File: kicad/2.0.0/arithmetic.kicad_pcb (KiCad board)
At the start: 2 copper layers, 38.4 x 55.2 mm, 69 parts, among them J1 Conn_01x03_Male, J2 Conn_01x05_Female, J3 Conn_01x05_Female, J4 Conn_Coaxial, J5 Conn_Coaxial, J6 Conn_Coaxial, U1 LM317, U2 LM337, U3 OPA2197xD, U4 OPA197xDBV

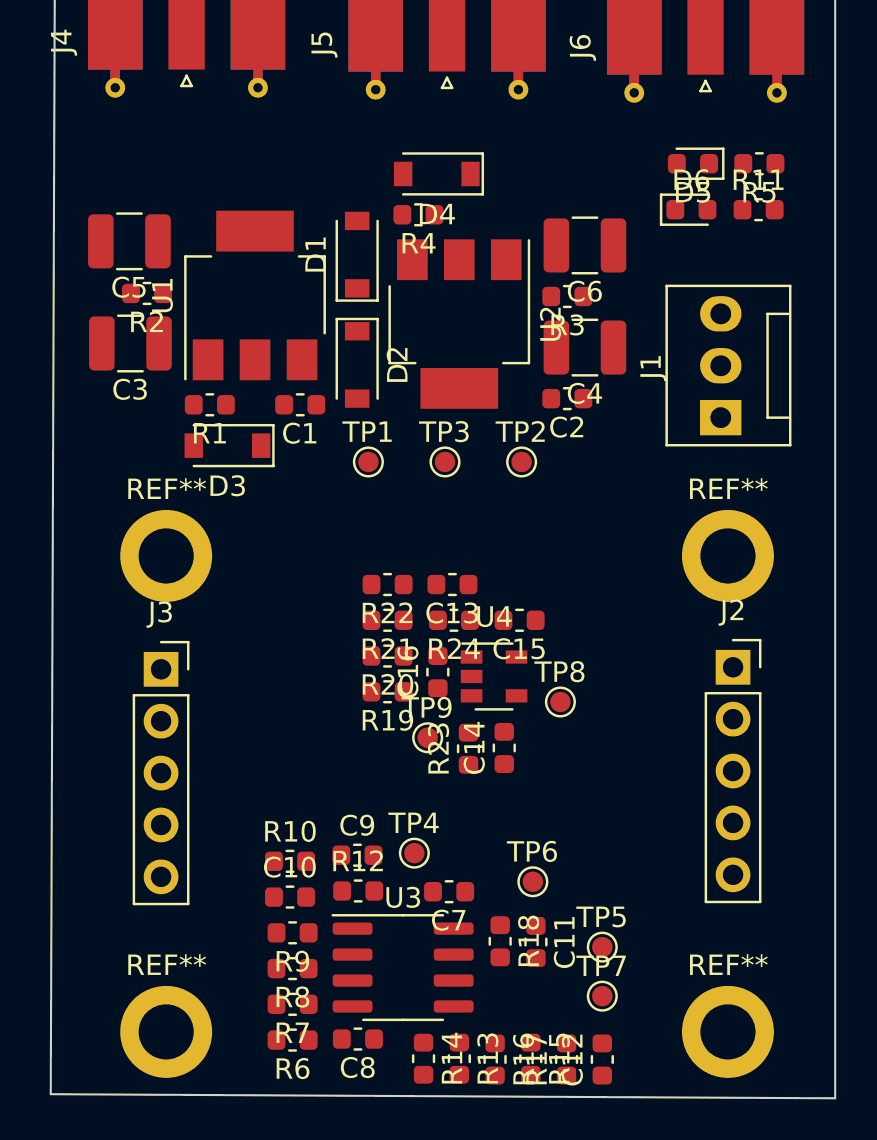
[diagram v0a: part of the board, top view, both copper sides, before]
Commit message: routed traces for 2.0.0 pcbs
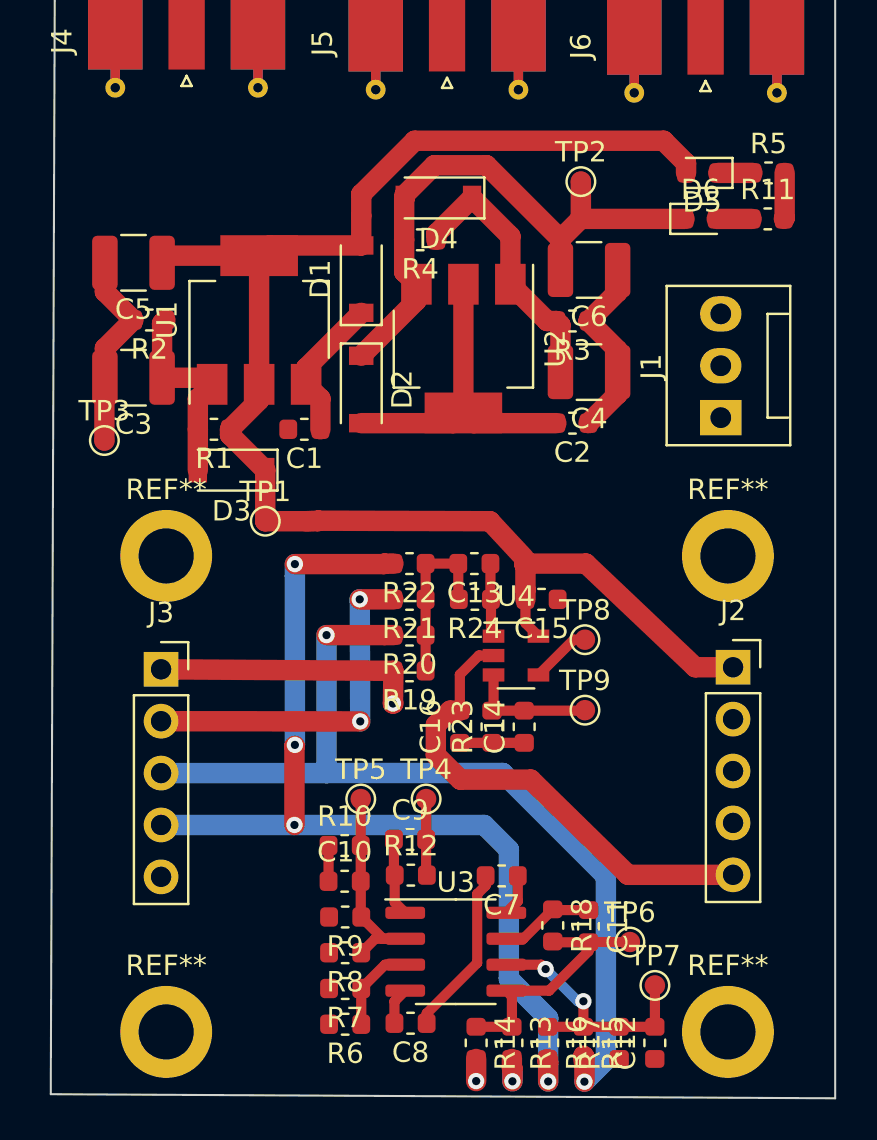
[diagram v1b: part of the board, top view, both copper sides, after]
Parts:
- moved TP3 16.7 mm to (201.2, 82.4)
- moved TP2 14.0 mm to (224.6, 69.7)
- moved TP5 13.9 mm to (213.8, 100.0)
- moved TP9 7.82 mm to (224.8, 95.6)
- moved TP1 5.82 mm to (209.1, 86.3)
- moved TP6 5.59 mm to (226.9, 107.0)
- moved TP8 3.28 mm to (224.8, 92.2)
- moved C16 2.88 mm to (218.6, 96.4)
- moved C10 2.79 mm to (213.0, 104.0)
- moved R10 2.79 mm to (213.0, 102.2)
- moved TP4 2.71 mm to (217.0, 100.0)
- moved R16 2.70 mm to (222.9, 111.9)
- moved R17 2.70 mm to (226.4, 111.9)
- moved C12 2.70 mm to (228.2, 111.9)
- moved C11 2.69 mm to (224.9, 106.2)
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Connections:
- J3 pad 2: /-X2 -> /-Y1
- J3 pad 3: /-Y1 -> /-X2
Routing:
- net +12V: track 0.00 -> 77.2 mm
- net -12V: track 0.00 -> 54.3 mm
- net /-Y2: track 0.00 -> 48.4 mm, vias 0 -> 4
- net /-X2: track 0.00 -> 45.8 mm, vias 0 -> 2
- net GND: track 0.00 -> 34.7 mm
- net /-Y1: track 0.00 -> 18.5 mm, vias 0 -> 3
- net -15V: track 0.00 -> 16.3 mm
- net /-X1: track 0.00 -> 14.7 mm, vias 0 -> 2
- net Net-(C4-Pad2): track 0.00 -> 13.4 mm
- net Net-(C12-Pad2): track 0.00 -> 13.2 mm, vias 0 -> 2
- net Net-(C11-Pad2): track 0.00 -> 12.7 mm
- net Net-(C13-Pad2): track 0.00 -> 11.6 mm
- net Net-(C10-Pad2): track 0.00 -> 10.8 mm
- net Net-(C3-Pad1): track 0.00 -> 9.97 mm
- net Net-(C9-Pad2): track 0.00 -> 8.12 mm
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
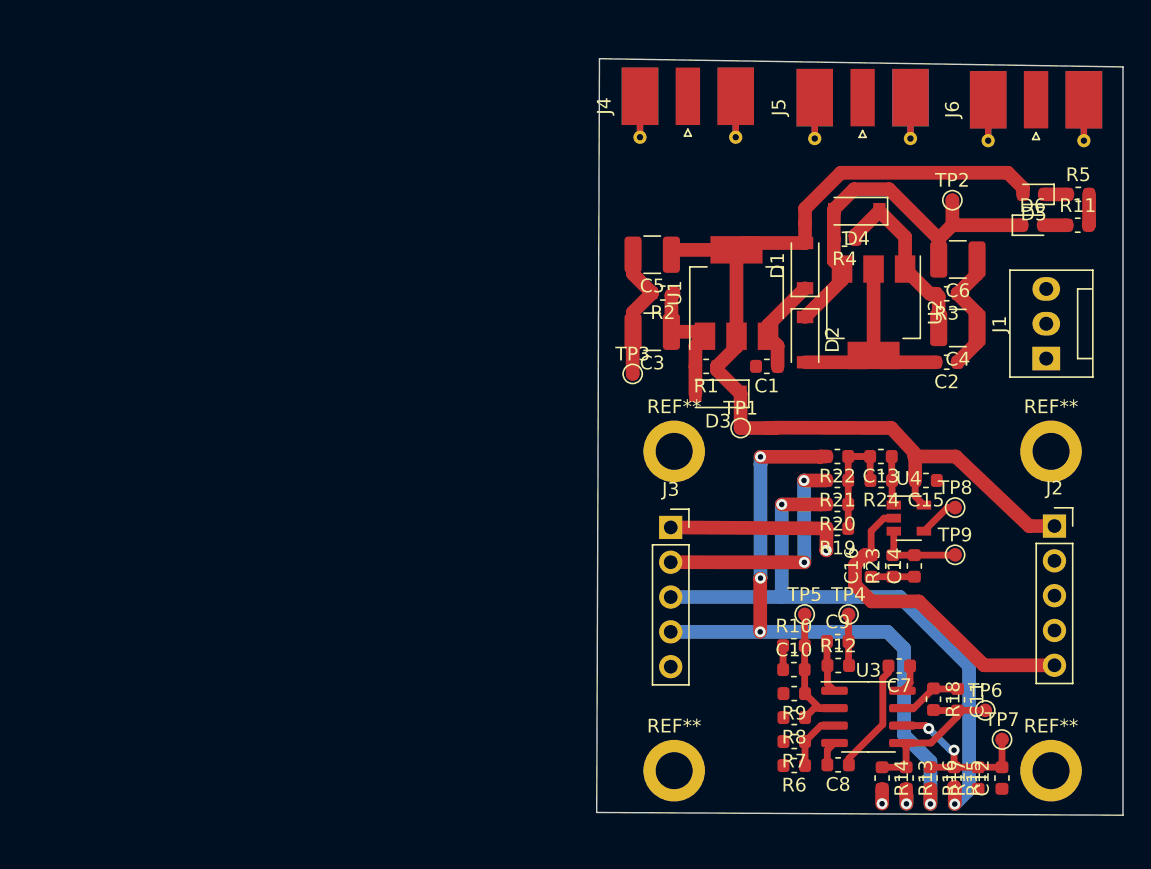
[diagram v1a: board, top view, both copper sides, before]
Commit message: replaced dual op-amp on 2.0.0 arithmetic board with two op-amps
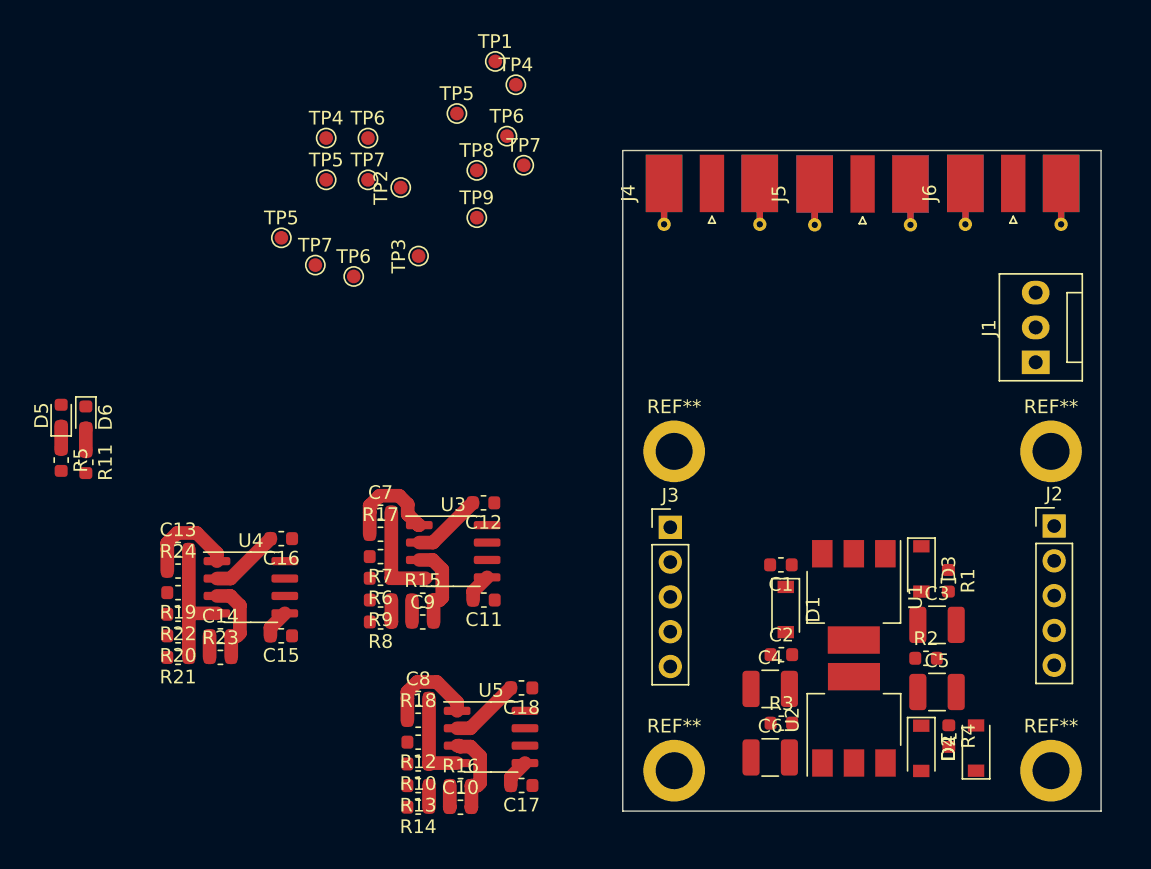
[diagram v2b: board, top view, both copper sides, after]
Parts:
- added C17: 100n, Capacitor_SMD:C_0603_1608Metric, F.Cu at (193.1, 112.4)
- added C18: 100n, Capacitor_SMD:C_0603_1608Metric, F.Cu at (193.1, 105.3)
- added TP4: DIFFX+, TestPoint:TestPoint_Pad_D1.0mm, F.Cu at (178.9, 65.2)
- added TP5: DIFFX-, TestPoint:TestPoint_Pad_D1.0mm, F.Cu at (175.6, 72.5)
- added TP5: DIFFY+, TestPoint:TestPoint_Pad_D1.0mm, F.Cu at (178.9, 68.2)
- added TP6: DIFFY-, TestPoint:TestPoint_Pad_D1.0mm, F.Cu at (180.9, 75.3)
- added TP6: DIFFX-, TestPoint:TestPoint_Pad_D1.0mm, F.Cu at (181.9, 65.2)
- added TP7: DIFFY+, TestPoint:TestPoint_Pad_D1.0mm, F.Cu at (178.1, 74.5)
- added TP7: DIFFY-, TestPoint:TestPoint_Pad_D1.0mm, F.Cu at (181.9, 68.2)
- added U5: OPA197xDBV, Package_SO:SOIC-8_3.9x4.9mm_P1.27mm, F.Cu at (190.9, 108.9)
- C11, C12: value 5p -> 100n
- C7, C8: value 100n -> 5p
- J2, J3: value Conn_01x05_Female -> Conn_01x05_Male; footprint Connector_PinSocket_2.54mm:PinSocket_1x05_P2.54mm_Vertical -> Connector_PinHeader_2.54mm:PinHeader_1x05_P2.54mm_Vertical
- U3: value OPA2197xD -> OPA197xDBV
- U4: footprint Package_TO_SOT_SMD:SOT-23-5 -> Package_SO:SOIC-8_3.9x4.9mm_P1.27mm
- moved R5 76.7 mm to (159.5, 88.7), turned to 270 degrees
- moved R11 74.4 mm to (161.3, 88.8), turned to 270 degrees
- moved D5 72.8 mm to (159.5, 85.4), turned to 90 degrees
- moved D6 70.5 mm to (161.3, 85.6), turned to 270 degrees
- moved TP7 54.5 mm to (193.3, 67.2)
- moved TP6 54.5 mm to (192.1, 65.0)
- moved R24 51.7 mm to (168.1, 96.8), turned to 0 degrees
- moved C13 51.7 mm to (168.1, 95.2), turned to 0 degrees
- moved C14 50.9 mm to (171.1, 101.5), turned to 0 degrees
- moved R21 49.8 mm to (168.1, 103.1)
- moved R23 49.5 mm to (171.1, 103.1), turned to 0 degrees
- moved R22 49.5 mm to (168.1, 99.9)
- moved R20 49.1 mm to (168.1, 101.5)
- moved C15 48.4 mm to (175.6, 101.5)
- moved R19 48.3 mm to (168.1, 98.4)
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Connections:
- C11 pad 1: /DIFFY -> GND
- C11 pad 2: Net-(C11-Pad2) -> +12V
- C12 pad 2: Net-(C12-Pad2) -> -12V
- C7 pad 1: +12V -> /DIFFX
- C7 pad 2: GND -> Net-(C7-Pad2)
- C8 pad 1: GND -> /DIFFY
- C8 pad 2: -12V -> Net-(C8-Pad2)
- C9 pad 1: /DIFFX -> GND
- R10 pad 1: GND -> Net-(C8-Pad2)
- R10 pad 2: Net-(C10-Pad2) -> /-X2
- R12 pad 1: /DIFFX -> Net-(C8-Pad2)
- R12 pad 2: Net-(C9-Pad2) -> /-Y2
- R13 pad 1: Net-(C11-Pad2) -> Net-(C10-Pad2)
- R14 pad 1: Net-(C11-Pad2) -> Net-(C10-Pad2)
- R15 pad 1: Net-(C12-Pad2) -> GND
- R15 pad 2: /-X2 -> Net-(C9-Pad2)
- R16 pad 1: Net-(C12-Pad2) -> GND
- R16 pad 2: /-Y2 -> Net-(C10-Pad2)
- R17 pad 1: GND -> /DIFFX
- R17 pad 2: Net-(C12-Pad2) -> Net-(C7-Pad2)
- R18 pad 2: Net-(C11-Pad2) -> Net-(C8-Pad2)
- R6 pad 1: Net-(C9-Pad2) -> Net-(C7-Pad2)
- R6 pad 2: /-X1 -> /-X2
- R7 pad 1: Net-(C9-Pad2) -> Net-(C7-Pad2)
- R7 pad 2: /-Y2 -> /-Y1
- R8 pad 1: Net-(C10-Pad2) -> Net-(C9-Pad2)
- R8 pad 2: /-X2 -> /-X1
- R9 pad 1: Net-(C10-Pad2) -> Net-(C9-Pad2)
- R9 pad 2: /-Y1 -> /-Y2
- U3 pad 2: Net-(C10-Pad2) -> -12V
- U3 pad 4: -12V -> Net-(C7-Pad2)
- U3 pad 5: Net-(C11-Pad2) -> +12V
- U3 pad 6: Net-(C12-Pad2) -> (no net)
- U3 pad 7: /DIFFY -> (no net)
- U3 pad 8: +12V -> (no net)
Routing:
- net +12V: track 77.2 -> 6.22 mm
- net /-Y2: track 48.4 -> 0.00 mm, vias 4 -> 0
- net /-X2: track 45.8 -> 0.00 mm, vias 2 -> 0
- net -12V: track 54.3 -> 15.3 mm
- net GND: track 34.7 -> 4.75 mm
- net /-Y1: track 18.5 -> 0.00 mm, vias 3 -> 0
- net -15V: track 16.3 -> 0.00 mm
- net /-X1: track 14.7 -> 0.00 mm, vias 2 -> 0
- net Net-(C4-Pad2): track 13.4 -> 0.00 mm
- net Net-(C12-Pad2): track 13.2 -> 0.00 mm, vias 2 -> 0
- net Net-(C11-Pad2): track 12.7 -> 0.00 mm
- net Net-(C3-Pad1): track 9.97 -> 0.00 mm
- net Net-(C7-Pad2): track 0.00 -> 7.31 mm
- net +15V: track 7.11 -> 0.00 mm
- net Net-(C8-Pad2): track 0.00 -> 6.86 mm
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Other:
- board size 38.4 x 55.2 mm -> 34.9 x 48.2 mm

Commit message: improved arithmetic 2.0.0 pcb
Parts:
- removed the REF** at (204.2, 88.0)
- removed the REF** at (204.2, 111.3)
- removed the TP6 at (192.1, 65.0)
- removed the TP6 at (181.9, 65.2)
- removed the TP7 at (193.3, 67.2)
- removed the TP7 at (181.9, 68.2)
- added REF**: MountingHole_2.7mm_M2.5_ISO7380_Pad, MountingHole:MountingHole_2.7mm_M2.5_ISO7380_Pad, F.Cu at (78.0, 105.8)
- added REF**: MountingHole_2.7mm_M2.5_ISO7380_Pad, MountingHole:MountingHole_2.7mm_M2.5_ISO7380_Pad, F.Cu at (78.0, 129.2)
- added TP7: DIFFY-, TestPoint:TestPoint_Pad_D1.0mm, F.Cu at (112.7, 98.0)
- R1, R2, R3, R4: footprint Resistor_SMD:R_0603_1608Metric -> Resistor_SMD:R_1210_3225Metric
- TP4: value DIFFX+ -> DIFFX-
- TP5: value DIFFX- -> DIFFX+
- TP6: value DIFFY- -> DIFFY+
- TP7: value DIFFY+ -> DIFFY-
- TP8: value SUM+ -> SUM-
- TP9: value SUM- -> SUM+
- moved J6 147.1 mm to (82.3, 77.4)
- moved C3 136.6 mm to (87.3, 111.9), turned to 180 degrees
- moved C5 136.1 mm to (87.3, 105.3), turned to 180 degrees
- moved R2 135.4 mm to (87.3, 108.6), turned to 180 degrees
- moved D4 135.1 mm to (88.3, 127.5)
- moved R4 133.6 mm to (91.9, 126.8), turned to 0 degrees
- moved R1 133.1 mm to (92.0, 111.9), turned to 180 degrees
- moved D3 131.6 mm to (91.9, 114.8), turned to 180 degrees
- moved D2 128.8 mm to (98.1, 122.7)
- moved J3 127.5 mm to (77.7, 111.4)
- moved REF** 127.5 mm to (105.5, 129.2)
- moved REF** 127.5 mm to (105.5, 105.8)
- moved J2 127.5 mm to (105.7, 111.3)
- moved C6 126.9 mm to (85.5, 127.5), turned to 270 degrees
- moved J1 126.2 mm to (113.0, 127.3), turned to 0 degrees
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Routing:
- net /-Y2: track 0.00 -> 61.8 mm, vias 0 -> 3
- net /-Y1: track 0.00 -> 60.3 mm, vias 0 -> 3
- net /-X2: track 0.00 -> 58.1 mm, vias 0 -> 3
- net /-X1: track 0.00 -> 57.0 mm, vias 0 -> 3
- net +12V: track 6.22 -> 53.6 mm
- net -15V: track 0.00 -> 43.0 mm, vias 0 -> 2
- net +15V: track 0.00 -> 37.0 mm, vias 0 -> 2
- net -12V: track 15.3 -> 50.8 mm
- net GND: track 4.75 -> 32.5 mm
- net Net-(C4-Pad2): track 0.00 -> 15.9 mm
- net Net-(C3-Pad1): track 0.00 -> 13.7 mm
- net /SUM: track 7.16 -> 14.4 mm
- net /DIFFY: track 7.23 -> 14.4 mm
- net /DIFFX: track 7.32 -> 14.4 mm
- net Net-(C9-Pad2): track 7.91 -> 11.8 mm
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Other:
- board size 34.9 x 48.2 mm -> 50 x 55 mm

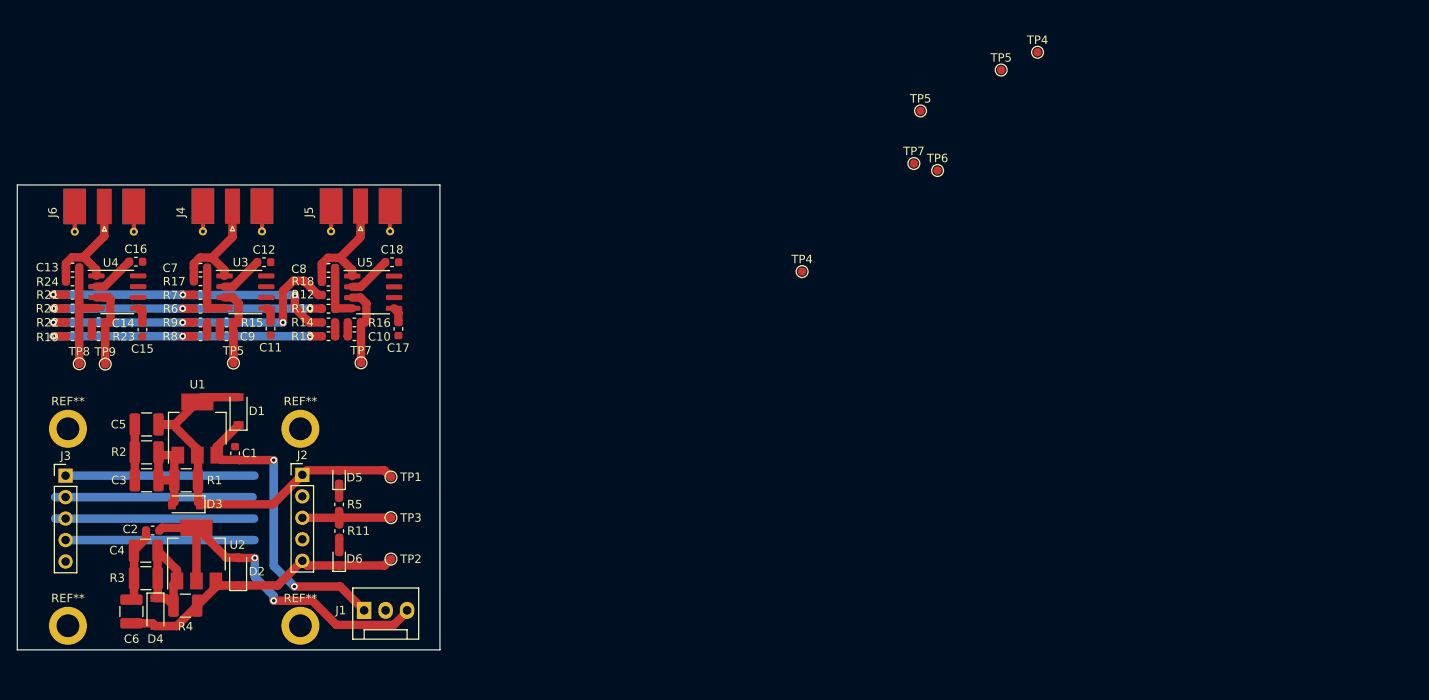
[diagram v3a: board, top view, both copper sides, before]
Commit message: completed signal tracing for arithmetic 2.0.0 board
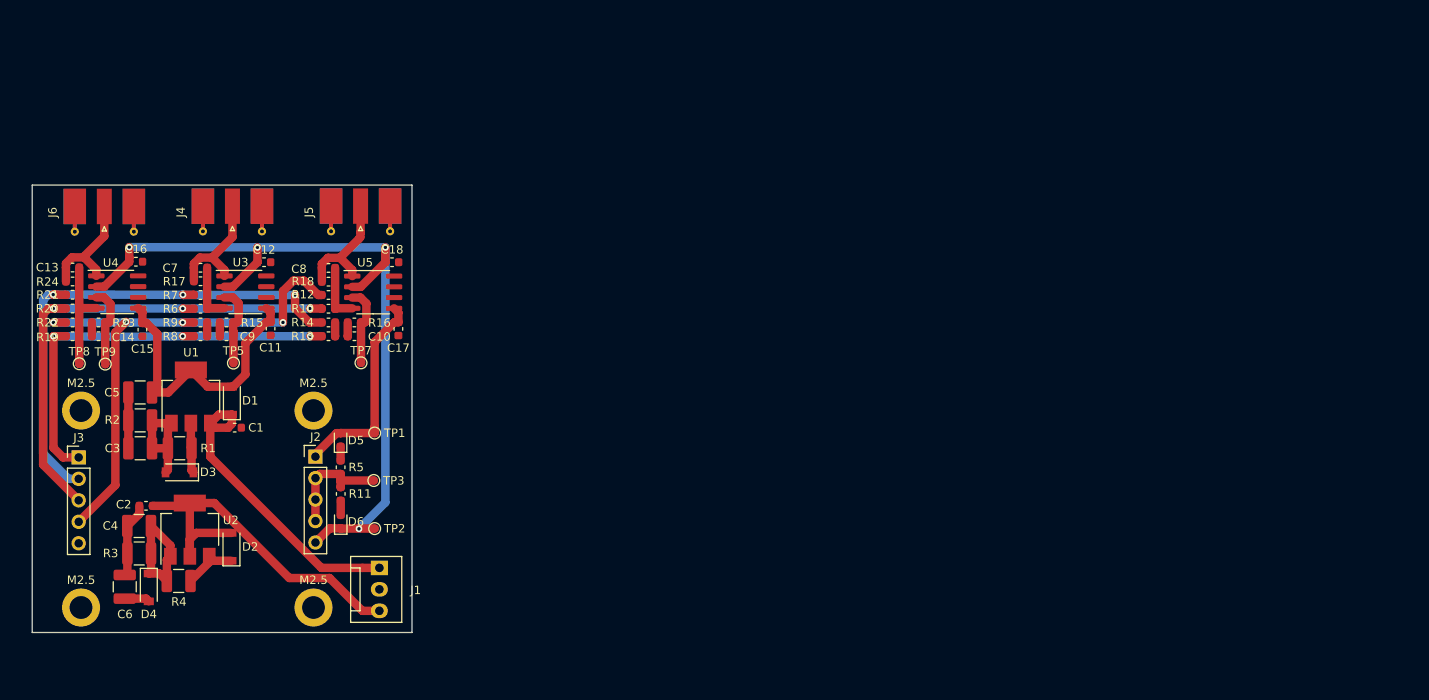
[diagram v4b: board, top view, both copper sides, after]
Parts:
- removed TP4: DIFFX-, TestPoint:TestPoint_Pad_D1.0mm
- removed TP4: DIFFX+, TestPoint:TestPoint_Pad_D1.0mm
- removed the TP5 at (188.4, 63.4)
- removed the TP5 at (178.9, 68.2)
- removed TP6: DIFFY+, TestPoint:TestPoint_Pad_D1.0mm
- removed the TP7 at (178.1, 74.5)
- moved TP1 5.55 mm to (114.3, 106.3)
- moved J1 5.34 mm to (114.8, 122.3), turned to 270 degrees
- moved TP3 4.84 mm to (114.2, 112.0)
- moved D5 4.40 mm to (110.2, 107.1)
- moved D6 4.40 mm to (110.3, 116.8)
- moved R11 4.40 mm to (110.3, 113.5)
- moved R5 4.40 mm to (110.2, 110.4)
- moved TP2 4.09 mm to (114.3, 117.7)
- moved C3 3.86 mm to (86.5, 108.2)
- moved C5 3.86 mm to (86.5, 101.5)
- moved R1 3.86 mm to (91.2, 108.2)
- moved R2 3.86 mm to (86.5, 104.9)
- moved U1 3.86 mm to (92.5, 102.0)
- moved D3 3.86 mm to (91.2, 111.0)
- moved C4 3.03 mm to (86.4, 117.3)
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- renumbered REF** to M2.5
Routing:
- net -12V: track 50.8 -> 102.9 mm, vias 0 -> 4
- net +12V: track 53.6 -> 65.3 mm
- net /-X1: track 57.0 -> 51.3 mm
- net /-Y2: track 61.8 -> 65.8 mm, vias 3 -> 4
- net -15V: track 43.0 -> 45.8 mm, vias 2 -> 0
- net /-X2: track 58.1 -> 59.9 mm
- net /-Y1: track 60.3 -> 62.0 mm
- net GND: track 32.5 -> 34.2 mm
- net +15V: track 37.0 -> 36.4 mm, vias 2 -> 0
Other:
- board size 50 x 55 mm -> 44.9 x 52.9 mm
